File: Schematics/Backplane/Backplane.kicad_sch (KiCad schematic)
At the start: 23 parts, among them J1 Edge Connector (SLOT 1), J2 Edge Connector (SLOT 2), J3 Edge Connector (SLOT 3), J4 Edge Connector (SLOT 4), J5 Edge Connector (SLOT 5), J6 Conn_01x06_Socket

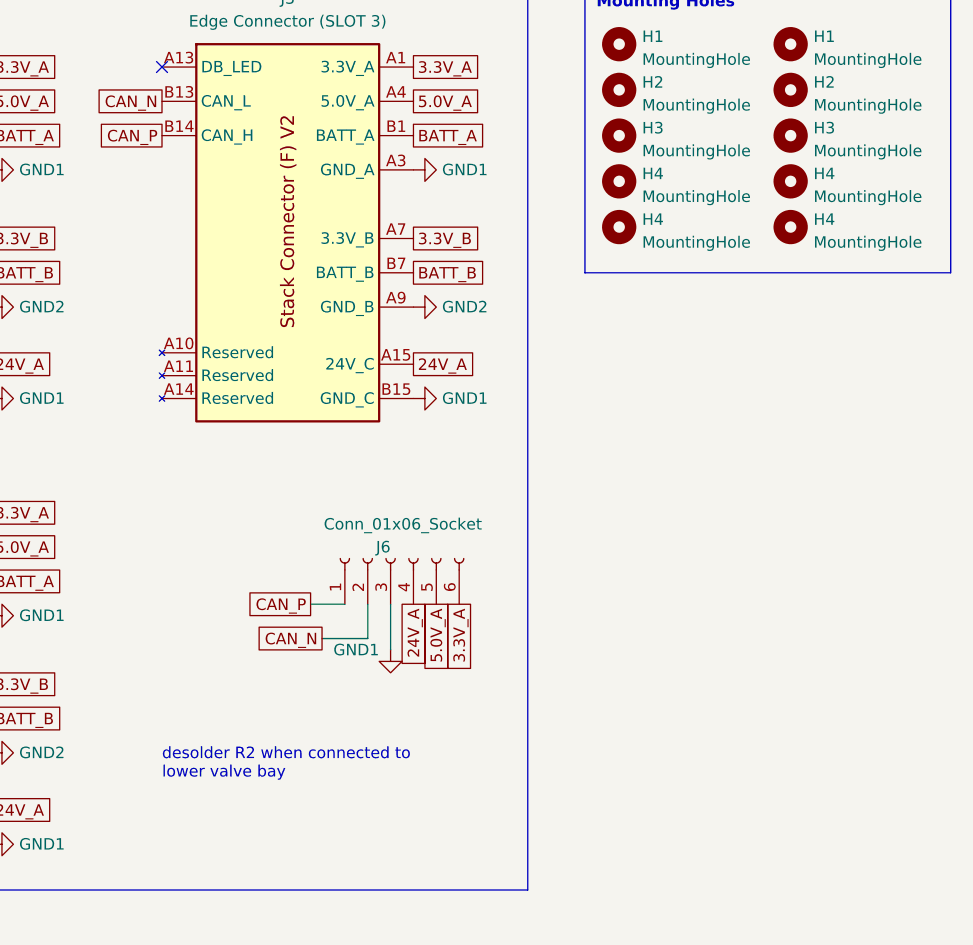
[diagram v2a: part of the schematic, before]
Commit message: updated backplane length to fit in stack design  - need to route traces to extension connector
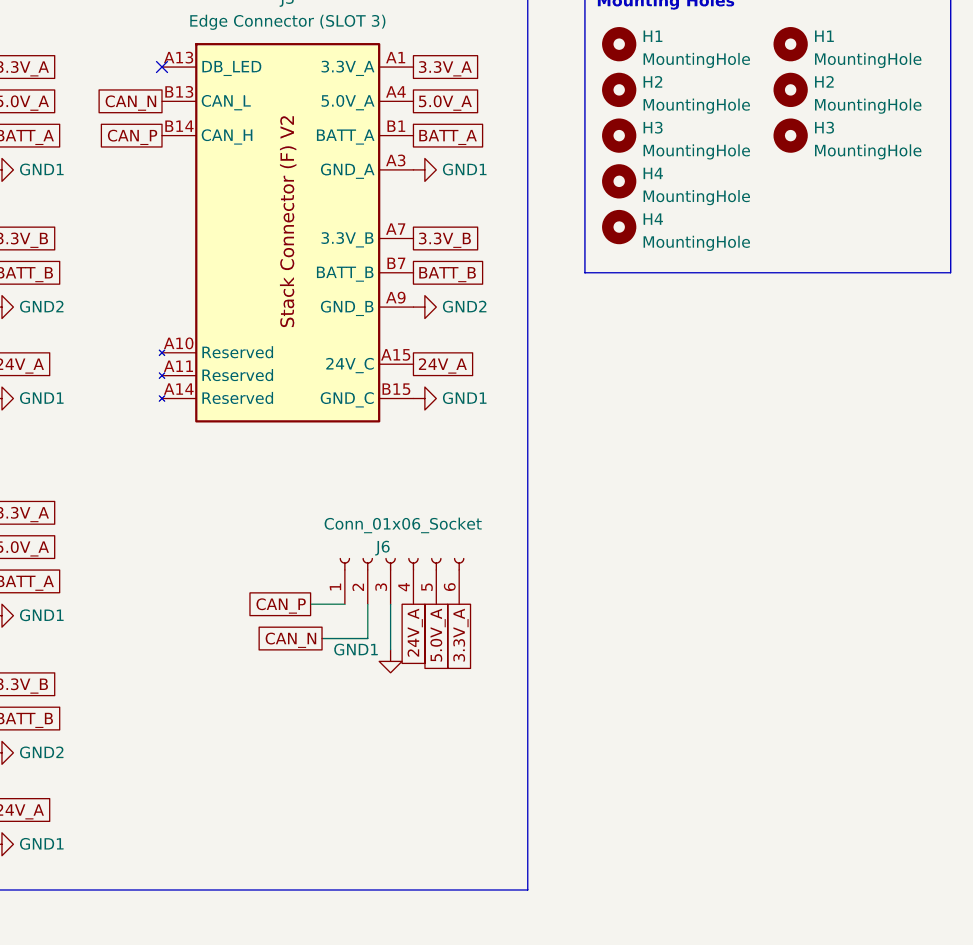
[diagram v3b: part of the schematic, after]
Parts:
- removed H4 (x2): MountingHole, MountingHole:MountingHole_3.2mm_M3_ISO14580_Pad, symbol Mechanical:MountingHole
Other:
- note removed: "desolder R2 when connected to lower valve bay"
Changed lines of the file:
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@@
 		)
 	)
-	(text "desolder R2 when connected to\nlower valve bay"
-		(exclude_from_sim no)
-		(at 116.84 101.6 0)
-		(effects
-			(font
-				(size 1.27 1.27)
-			)
-			(justify left)
-		)
-	)
 	(text "Cut bridge trace when\nconnected to lower valve bay"
 		(exclude_from_sim no)
@@
 	)
 	(symbol
-		(lib_id "Mechanical:MountingHole")
-		(at 186.69 41.91 0)
-		(unit 1)
-		(exclude_from_sim no)
-		(in_bom no)
-		(on_board yes)
-		(dnp no)
-		(fields_autoplaced yes)
-		(property "Reference" "H4"
-			(at 189.23 41.0753 0)
-			(effects
-				(font
-					(size 1.27 1.27)
-				)
-				(justify left)
-			)
-		)
-		(property "Value" "MountingHole"
-			(at 189.23 43.6122 0)
-			(effects
-				(font
-					(size 1.27 1.27)
-				)
-				(justify left)
-			)
-		)
-		(property "Footprint" "MountingHole:MountingHole_3.2mm_M3_ISO14580_Pad"
-			(at 186.69 41.91 0)
-			(effects
-				(font
-					(size 1.27 1.27)
-				)
-				(hide yes)
-			)
-		)
-		(property "Datasheet" "~"
-			(at 186.69 41.91 0)
-			(effects
-				(font
-					(size 1.27 1.27)
-				)
-				(hide yes)
-			)
-		)
-		(property "Description" ""
-			(at 186.69 41.91 0)
-			(effects
-				(font
-					(size 1.27 1.27)
-				)
-				(hide yes)
-			)
-		)
-		(instances
-			(project "Vector PCB"
-				(path "/2c1d7b44-b9fb-4113-ba6e-9cd5044a1dfb"
-					(reference "H4")
-					(unit 1)
-				)
-			)
-			(project "Backplane"
-				(path "/d6cecfea-6157-498d-8796-49576704a9cc"
-					(reference "H10")
-					(unit 1)
-				)
-			)
-		)
-	)
-	(symbol
 		(lib_id "power:GND1")
 		(at 52.07 36.83 90)
@@
 					(unit 1)
 				)
-			)
-		)
-	)
-	(symbol
-		(lib_id "Mechanical:MountingHole")
-		(at 186.69 36.83 0)
-		(unit 1)
-		(exclude_from_sim no)
-		(in_bom no)
-		(on_board yes)
-		(dnp no)
-		(fields_autoplaced yes)
-		(property "Reference" "H4"
-			(at 189.23 35.9953 0)
-			(effects
-				(font
-					(size 1.27 1.27)
-				)
-				(justify left)
-			)
-		)
-		(property "Value" "MountingHole"
-			(at 189.23 38.5322 0)
-			(effects
-				(font
-					(size 1.27 1.27)
-				)
-				(justify left)
-			)
-		)
-		(property "Footprint" "MountingHole:MountingHole_3.2mm_M3_ISO14580_Pad"
-			(at 186.69 36.83 0)
-			(effects
-				(font
-					(size 1.27 1.27)
-				)
-				(hide yes)
-			)
-		)
-		(property "Datasheet" "~"
-			(at 186.69 36.83 0)
-			(effects
-				(font
-					(size 1.27 1.27)
-				)
-				(hide yes)
-			)
-		)
-		(property "Description" ""
-			(at 186.69 36.83 0)
-			(effects
-				(font
-					(size 1.27 1.27)
-				)
-				(hide yes)
-			)
-		)
-		(instances
-			(project "Vector PCB"
-				(path "/2c1d7b44-b9fb-4113-ba6e-9cd5044a1dfb"
-					(reference "H4")
-					(unit 1)
-				)
-			)
-			(project "Backplane"
-				(path "/d6cecfea-6157-498d-8796-49576704a9cc"
-					(reference "H9")
-					(unit 1)
-				)

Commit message: start of my own backplane layout
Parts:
- removed J1: Edge Connector (SLOT 1), footprints:AMPHENOL_10018784-10210TLF, symbol EdgeConnnectorV1.1:Stack Female Edge Connector
- removed J2: Edge Connector (SLOT 2), footprints:AMPHENOL_10018784-10210TLF, symbol EdgeConnnectorV1.1:Stack Female Edge Connector
- removed J3: Edge Connector (SLOT 3), footprints:AMPHENOL_10018784-10210TLF, symbol EdgeConnnectorV1.1:Stack Female Edge Connector
- removed J4: Edge Connector (SLOT 4), footprints:AMPHENOL_10018784-10210TLF, symbol EdgeConnnectorV1.1:Stack Female Edge Connector
- removed J5: Edge Connector (SLOT 5), footprints:AMPHENOL_10018784-10210TLF, symbol EdgeConnnectorV1.1:Stack Female Edge Connector
- added J1: Edge Connector (SLOT 1), footprints:AMPHENOL_10018784-10210TLF, symbol EdgeConnnectorV2:Stack Female Edge Connector
- added J2: Edge Connector (SLOT 2), footprints:AMPHENOL_10018784-10210TLF, symbol EdgeConnnectorV2:Stack Female Edge Connector
- added J3: Edge Connector (SLOT 3), footprints:AMPHENOL_10018784-10210TLF, symbol EdgeConnnectorV2:Stack Female Edge Connector
- added J4: Edge Connector (SLOT 4), footprints:AMPHENOL_10018784-10210TLF, symbol EdgeConnnectorV2:Stack Female Edge Connector
- added J5: Edge Connector (SLOT 5), footprints:AMPHENOL_10018784-10210TLF, symbol EdgeConnnectorV2:Stack Female Edge Connector
- JP3: value SolderJumper_2_Bridged -> 3.3V Bridge
- JP4: value SolderJumper_2_Bridged -> BATT Bridge
- JP5: value SolderJumper_2_Bridged -> GND Bridge
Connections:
- net 24V_A: now also J1.A16 (24V_A), J1.A18 (24V_A), J2.A16 (24V_A), J2.A18 (24V_A), J3.A16 (24V_A), J3.A18 (24V_A), J4.A16 (24V_A), J4.A18 (24V_A), J5.A16 (24V_A), J5.A18 (24V_A)
- net 3.3V_A: now also J1.A1 (3.3V_A), J1.A2 (3.3V_A), J2.A1 (3.3V_A), J2.A2 (3.3V_A), J3.A1 (3.3V_A), J3.A2 (3.3V_A), J4.A1 (3.3V_A), J4.A2 (3.3V_A), J5.A1 (3.3V_A), J5.A2 (3.3V_A)
- net 3.3V_B: now also J1.A7 (3.3V_B), J1.A8 (3.3V_B), J2.A7 (3.3V_B), J2.A8 (3.3V_B), J3.A7 (3.3V_B), J3.A8 (3.3V_B), J4.A7 (3.3V_B), J4.A8 (3.3V_B), J5.A7 (3.3V_B), J5.A8 (3.3V_B)
- net 5.0V_A: now also J1.A4 (5.0V_A), J1.A5 (5.0V_A), J2.A4 (5.0V_A), J2.A5 (5.0V_A), J3.A4 (5.0V_A), J3.A5 (5.0V_A), J4.A4 (5.0V_A), J4.A5 (5.0V_A), J5.A4 (5.0V_A), J5.A5 (5.0V_A)
- net BATT_A: now also J1.B1 (BATT_A), J1.B2 (BATT_A), J1.B3 (BATT_A), J2.B1 (BATT_A), J2.B2 (BATT_A), J2.B3 (BATT_A), J3.B1 (BATT_A), J3.B2 (BATT_A), J3.B3 (BATT_A), J4.B1 (BATT_A), J4.B2 (BATT_A), J4.B3 (BATT_A), J5.B1 (BATT_A), J5.B2 (BATT_A), J5.B3 (BATT_A)
- net BATT_B: now also J1.B7 (BATT_B), J1.B8 (BATT_B), J1.B9 (BATT_B), J2.B7 (BATT_B), J2.B8 (BATT_B), J2.B9 (BATT_B), J3.B7 (BATT_B), J3.B8 (BATT_B), J3.B9 (BATT_B), J4.B7 (BATT_B), J4.B8 (BATT_B), J4.B9 (BATT_B), J5.B7 (BATT_B), J5.B8 (BATT_B), J5.B9 (BATT_B)
- net CAN_N: now also J1.B13 (CAN_L), J2.B13 (CAN_L), J3.B13 (CAN_L), J4.B13 (CAN_L), J5.B13 (CAN_L)
- net CAN_P: now also J6.3 (Pin_3), J1.B14 (CAN_H), J2.B14 (CAN_H), J3.B14 (CAN_H), J4.B14 (CAN_H), J5.B14 (CAN_H); no longer J6.1 (Pin_1)
- net GND1: now also J6.1 (Pin_1), J1.A3 (GND_A), J1.A6 (GND_A), J1.B4 (GND_A), J1.B5 (GND_A), J1.B6 (GND_A), J2.A3 (GND_A), J2.A6 (GND_A), J2.B4 (GND_A), J2.B5 (GND_A), J2.B6 (GND_A), J3.A3 (GND_A), J3.A6 (GND_A), J3.B4 (GND_A), J3.B5 (GND_A), J3.B6 (GND_A), J4.A3 (GND_A), J4.A6 (GND_A), J4.B4 (GND_A), J4.B5 (GND_A), J4.B6 (GND_A), J5.A3 (GND_A), J5.A6 (GND_A), J5.B4 (GND_A), J5.B5 (GND_A), J5.B6 (GND_A); no longer J6.3 (Pin_3)
- net GND2: now also J1.A12 (GND_B), J1.A9 (GND_B), J1.B10 (GND_B), J1.B11 (GND_B), J1.B12 (GND_B), J2.A12 (GND_B), J2.A9 (GND_B), J2.B10 (GND_B), J2.B11 (GND_B), J2.B12 (GND_B), J3.A12 (GND_B), J3.A9 (GND_B), J3.B10 (GND_B), J3.B11 (GND_B), J3.B12 (GND_B), J4.A12 (GND_B), J4.A9 (GND_B), J4.B10 (GND_B), J4.B11 (GND_B), J4.B12 (GND_B), J5.A12 (GND_B), J5.A9 (GND_B), J5.B10 (GND_B), J5.B11 (GND_B), J5.B12 (GND_B)
